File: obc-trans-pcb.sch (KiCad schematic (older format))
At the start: 7 parts

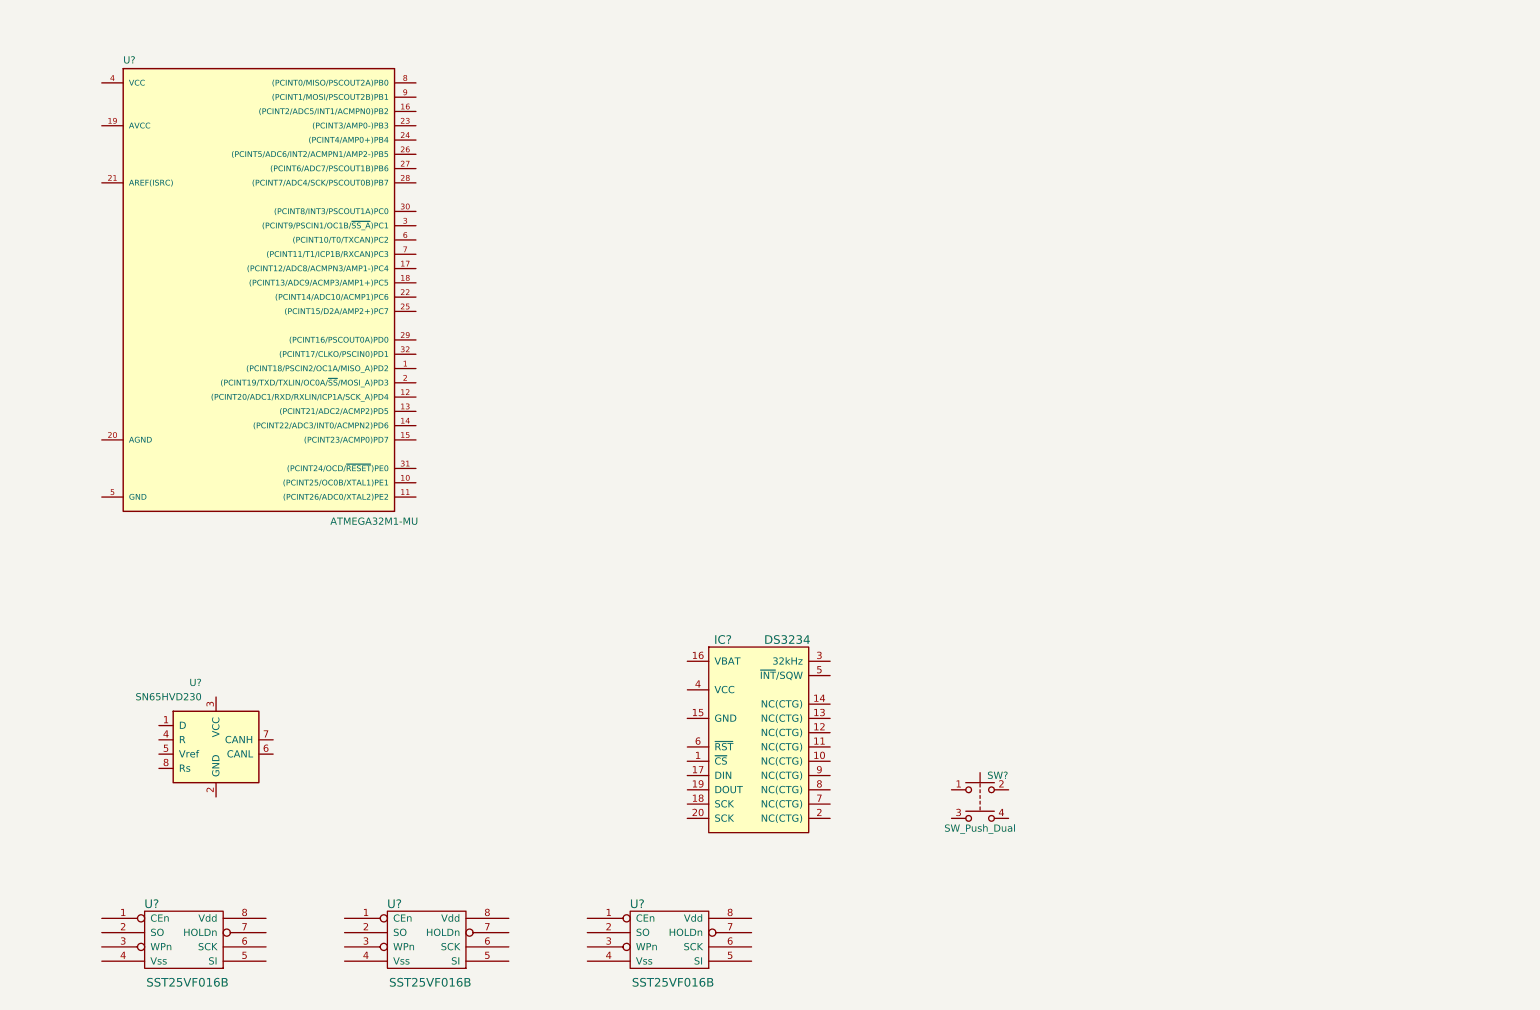
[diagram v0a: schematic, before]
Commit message: some changes
added some nets. current remaining
schematic needs:
* add connectors
* create & add footprint for transceiver
* add power nets for MCU
* confirm all nets are in place
* do we need SCK/MOSI/MISO _A?
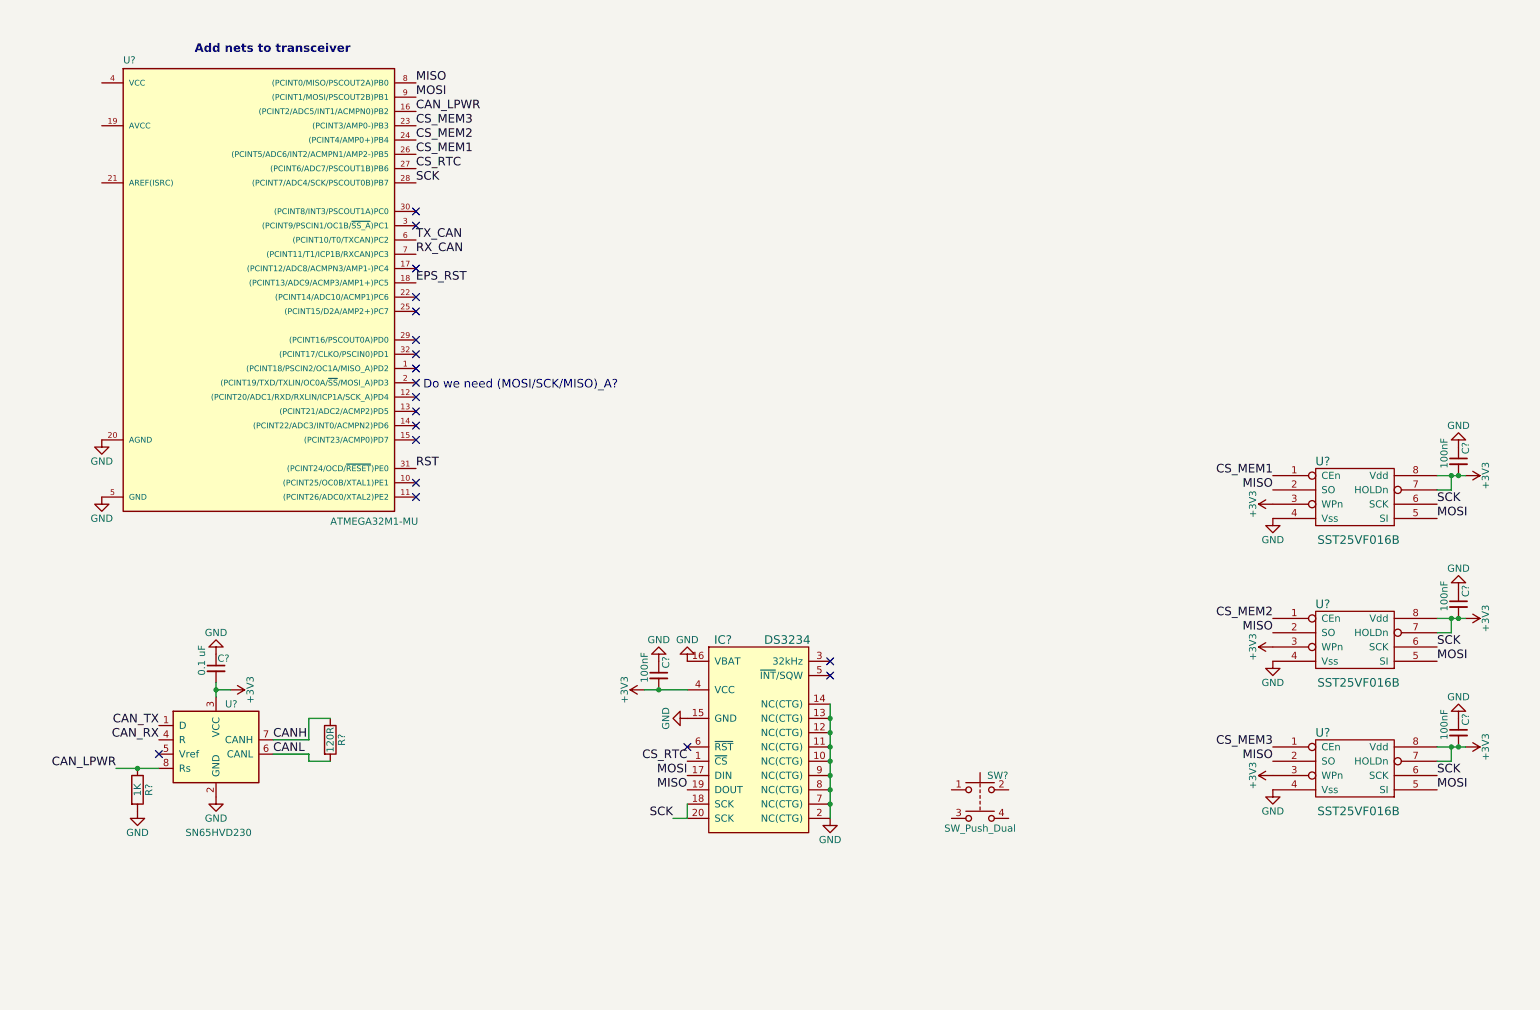
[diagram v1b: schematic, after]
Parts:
- removed U? (x2): SST25VF016B, symbol SST25VF016B
- added C? (x4): 100nF, symbol C_Small
- added C?: 0.1 uF, symbol C_Small
- added R?: 120R, symbol R
- added R?: 1K, symbol R
- added U? (x2): SST25VF016B, symbol SST25VF016B
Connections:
- net CAN_LPWR: now reaches U?.16 ((PCINT2/ADC5/INT1/ACMPN0)PB2)
- net CAN_LPWR: now also U?.8 (Rs), R?.1
- net EPS_RST: now reaches U?.18 ((PCINT13/ADC9/ACMP3/AMP1+)PC5)
- net GND: now reaches U?.20 (AGND)
- net GND: now also IC?.10 (NC(CTG)), IC?.11 (NC(CTG)), IC?.12 (NC(CTG)), IC?.13 (NC(CTG)), IC?.14 (NC(CTG)), IC?.15 (GND), IC?.16 (VBAT), IC?.2 (NC(CTG)), IC?.7 (NC(CTG)), IC?.8 (NC(CTG)), IC?.9 (NC(CTG)), U?.2 (GND), U?.4 (Vss), U?.5 (GND), C?.1, C?.1, C?.1, C?.1, C?.1, R?.2, U?.4 (Vss), U?.4 (Vss)
- net CS_MEM3: now reaches U?.23 ((PCINT3/AMP0-)PB3)
- net CS_MEM3: now also U?.1 (CEn)
- net CS_MEM2: now reaches U?.24 ((PCINT4/AMP0+)PB4)
- net CS_MEM2: now also U?.1 (CEn)
- net CS_MEM1: now reaches U?.26 ((PCINT5/ADC6/INT2/ACMPN1/AMP2-)PB5)
- net CS_MEM1: now also U?.1 (CEn)
- net CS_RTC: now reaches U?.27 ((PCINT6/ADC7/PSCOUT1B)PB6)
- net CS_RTC: now also IC?.1 (~CS~)
- net SCK: now reaches U?.28 ((PCINT7/ADC4/SCK/PSCOUT0B)PB7)
- net SCK: now also IC?.18 (SCK), IC?.20 (SCK), U?.6 (SCK), U?.6 (SCK), U?.6 (SCK)
- net RST: now reaches U?.31 ((PCINT24/OCD/~RESET~)PE0)
- net TX_CAN: now reaches U?.6 ((PCINT10/T0/TXCAN)PC2)
- net RX_CAN: now reaches U?.7 ((PCINT11/T1/ICP1B/RXCAN)PC3)
- net MISO: now reaches U?.8 ((PCINT0/MISO/PSCOUT2A)PB0)
- net MISO: now also IC?.19 (DOUT), U?.2 (SO), U?.2 (SO), U?.2 (SO)
- net MOSI: now reaches U?.9 ((PCINT1/MOSI/PSCOUT2B)PB1)
- net MOSI: now also IC?.17 (DIN), U?.5 (SI), U?.5 (SI), U?.5 (SI)
- net +3V3: now reaches U?.3 (WPn)
- net +3V3: now also IC?.4 (VCC), U?.3 (VCC), U?.7 (HOLDn), U?.8 (Vdd), C?.2, C?.2, C?.2, C?.2, C?.2, U?.3 (WPn), U?.3 (WPn), U?.7 (HOLDn), U?.7 (HOLDn), U?.8 (Vdd), U?.8 (Vdd)
- net CAN_TX: now reaches U?.1 (D)
- net CAN_RX: now reaches U?.4 (R)
- net CANL: now reaches U?.6 (CANL)
- net CANL: now also R?.2
- net CANH: now reaches U?.7 (CANH)
- net CANH: now also R?.1
- no-connect marks 0 -> 19
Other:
- note added: "Add nets to transceiver"
- note added: "Do we need (MOSI/SCK/MISO)_A?"
- moved on the sheet: U?

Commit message: basically finished schematic :(
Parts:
- added C1, C2, C3: 0.1 uF, Capacitors_SMD:C_0603_HandSoldering, symbol C
- added C8, C9: 22pF, Capacitors_SMD:C_0603_HandSoldering, symbol C_Small
- added J1: H1, Pin_Headers:Pin_Header_Straight_2x26_Pitch2.54mm_SMD, symbol Conn_02x26_Odd_Even
- added J2: H2, Pin_Headers:Pin_Header_Straight_2x26_Pitch2.54mm_SMD, symbol Conn_02x26_Odd_Even
- added J3: H_EPS, Pin_Headers:Pin_Header_Straight_2x05_Pitch2.54mm_SMD, symbol Conn_02x05_Odd_Even
- added R3: 10K, Resistors_SMD:R_0603, symbol R
- added R4, R5: 0R, Resistors_SMD:R_0603, symbol R
- added Y1: 8 MHz, Crystals:Crystal_SMD_Abracon_ABM3B-4pin_5.0x3.2mm, symbol Crystal_GND24
- C10, C4, C5, C6, C7: renamed from C?; footprint (none) -> Capacitors_SMD:C_0603_HandSoldering
- IC1: renamed from IC?; footprint (none) -> Housings_SOIC:SOIC-20W_7.5x12.8mm_Pitch1.27mm
- R1, R2: renamed from R?; footprint (none) -> Resistors_SMD:R_0603
- SW1: renamed from SW?; value SW_Push_Dual -> SW_RST
- U2: renamed from U?; footprint QFN32 -> Housings_QFP:TQFP-32_7x7mm_Pitch0.8mm
- U3, U4, U5: renamed from U?; footprint (none) -> Housings_SOIC:SO-8_5.3x6.2mm_Pitch1.27mm
- gave numbers to parts that had none: 1
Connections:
- net +3V3: now also U2.19 (AVCC), U2.21 (AREF(ISRC)), U2.4 (VCC), C1.2, C2.2, C3.2, J2.27 (Pin_27), J2.28 (Pin_28), J3.1 (Pin_1), R3.1
- net CANH: now also J3.5 (Pin_5)
- net CANL: now also J3.7 (Pin_7)
- net EPS_RST: now also J3.8 (Pin_8)
- net GND: now also SW1.2, SW1.4, C1.1, C2.1, C3.1, C8.1, C9.1, J2.29 (Pin_29), J2.30 (Pin_30), J2.31 (Pin_31), J2.32 (Pin_32), J3.10 (Pin_10), J3.9 (Pin_9), Y1.2, Y1.4
- net RST: now also SW1.1, SW1.3, R3.2
- net MISO_A: now reaches U2.1 ((PCINT18/PSCIN2/OC1A/MISO_A)PD2)
- net at U2.10 ((PCINT25/OC0B/XTAL1)PE1): now also C8.2, Y1.1
- net at U2.11 ((PCINT26/ADC0/XTAL2)PE2): now also C9.2, Y1.3
- net SCK_A: now reaches U2.12 ((PCINT20/ADC1/RXD/RXLIN/ICP1A/SCK_A)PD4)
- net SCK_A: now also R4.2
- net MOSI_A: now reaches U2.2 ((PCINT19/TXD/TXLIN/OC0A/~SS~/MOSI_A)PD3)
- net MOSI_A: now also R5.2
- net EN_UHF: now reaches U2.25 ((PCINT15/D2A/AMP2+)PC7)
- net EN_UHF: now also J2.7 (Pin_7)
- new net +5V: J2.25 (Pin_25), J2.26 (Pin_26), J3.2 (Pin_2)
- new net COM_RXD: J1.33 (Pin_33), R4.1
- new net COM_TXD: J1.35 (Pin_35), R5.1
- no-connect marks 19 -> 16
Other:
- note added: "Decisions:\n* Don't connect I2C or CAN\n* Don't connect RS485 (H1-22&24), b/c we're using UART\n* Ignoring latch-up protection (H1-48)"
- note removed: "Add nets to transceiver"
- note removed: "Do we need (MOSI/SCK/MISO)_A?"
- moved on the sheet: C10, C4, C5, C6, C7, IC1, R1, R2, SW1, U1, U2, U3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

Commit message: actually done sch
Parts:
- C1, C2, C3, C4: value 0.1 uF -> 100nF
- SW1: footprint (none) -> Buttons_Switches_SMD:SW_SPST_B3S-1000

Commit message: actually done fr
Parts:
- added D1: PWR_LED, LEDs:LED_0603, symbol LED
- added J4: DEBUGGING PORT, Pin_Headers:Pin_Header_Straight_2x03_Pitch2.54mm_SMD, symbol Conn_02x03_Odd_Even
- added J5: PROGRAMMING PORT, Pin_Headers:Pin_Header_Straight_2x03_Pitch2.54mm_SMD, symbol Conn_02x03_Odd_Even
- added R6: 120R, Resistors_SMD:R_0603, symbol R
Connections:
- net RX_CAN is gone; now on net CAN_RX: U2.7 ((PCINT11/T1/ICP1B/RXCAN)PC3)
- net TX_CAN is gone; now on net CAN_TX: U2.6 ((PCINT10/T0/TXCAN)PC2)
- net +3V3: now also J4.1 (Pin_1), J4.2 (Pin_2), J5.2 (Pin_2), R6.1
- net GND: now also D1.1 (K), J4.5 (Pin_5), J4.6 (Pin_6), J5.6 (Pin_6)
- net MISO_A: now also J5.1 (Pin_1)
- net MOSI_A: now also J4.3 (Pin_3), J5.4 (Pin_4)
- net RST: now also J5.5 (Pin_5)
- net SCK_A: now also J4.4 (Pin_4), J5.3 (Pin_3)
- new net: D1.2 (A), R6.2
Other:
- moved on the sheet: R3, SW1

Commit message: v1 layout, without GND & 3V3 planes
Everything should be connected. Sorry it looks uggles :(
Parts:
- J1, J2: footprint Pin_Headers:Pin_Header_Straight_2x26_Pitch2.54mm_SMD -> Pin_Headers:Pin_Header_Straight_2x26_Pitch2.54mm
- J3: footprint Pin_Headers:Pin_Header_Straight_2x05_Pitch2.54mm_SMD -> Pin_Headers:Pin_Header_Straight_2x05_Pitch2.54mm
- J4, J5: footprint Pin_Headers:Pin_Header_Straight_2x03_Pitch2.54mm_SMD -> Pin_Headers:Pin_Header_Straight_2x03_Pitch2.54mm
